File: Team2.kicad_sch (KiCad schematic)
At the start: 71 parts, among them J1 Conn_01x05, J10 Conn_01x03_MountingPin, J11 Conn_01x03_MountingPin, J12 Conn_01x03_MountingPin, J13 Conn_01x03_MountingPin, J14 Conn_01x03_MountingPin, J15 Conn_01x03_Pin, J16 Conn_01x08_Pin, J17 XT60-M, J18 XT60-M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

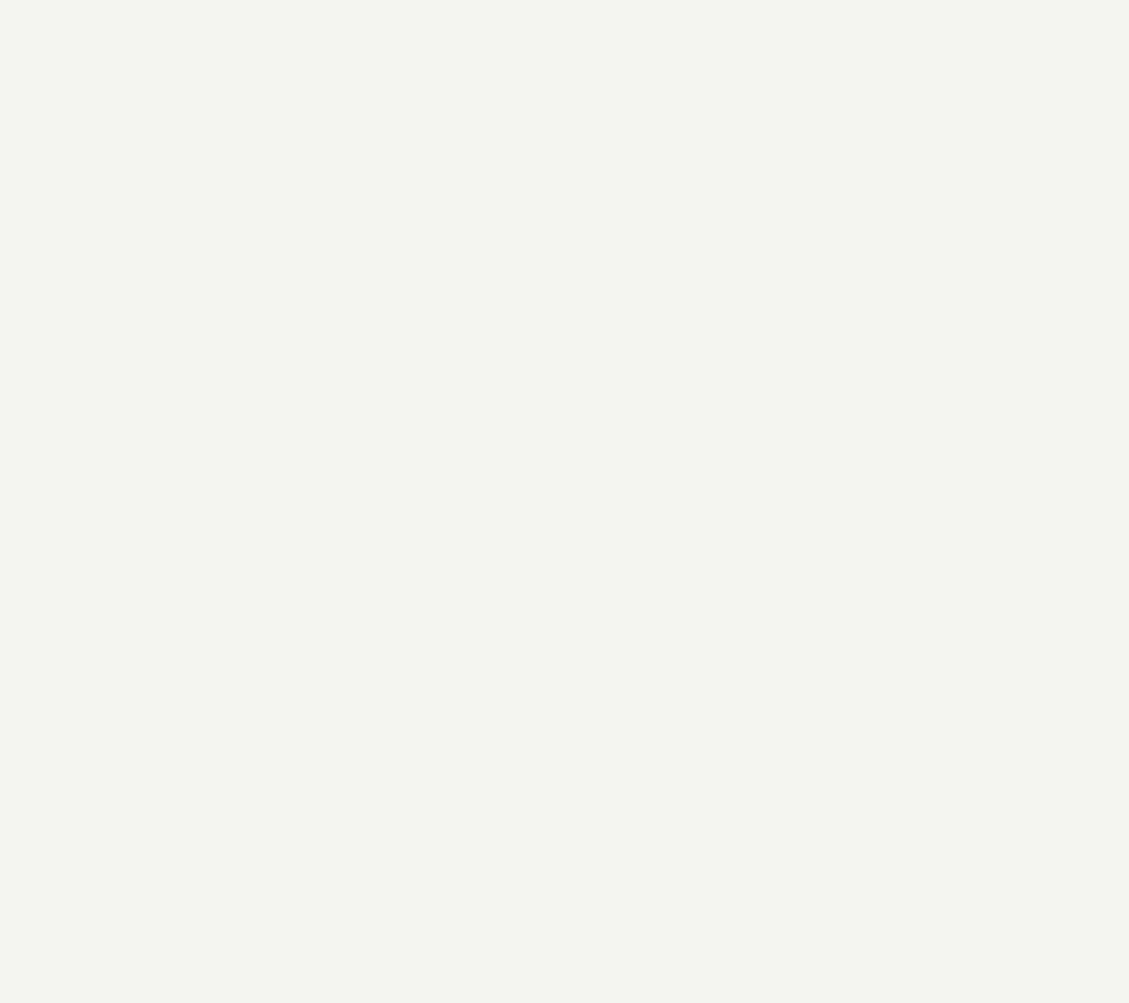
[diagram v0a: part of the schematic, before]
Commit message: schematic with vol. reg.
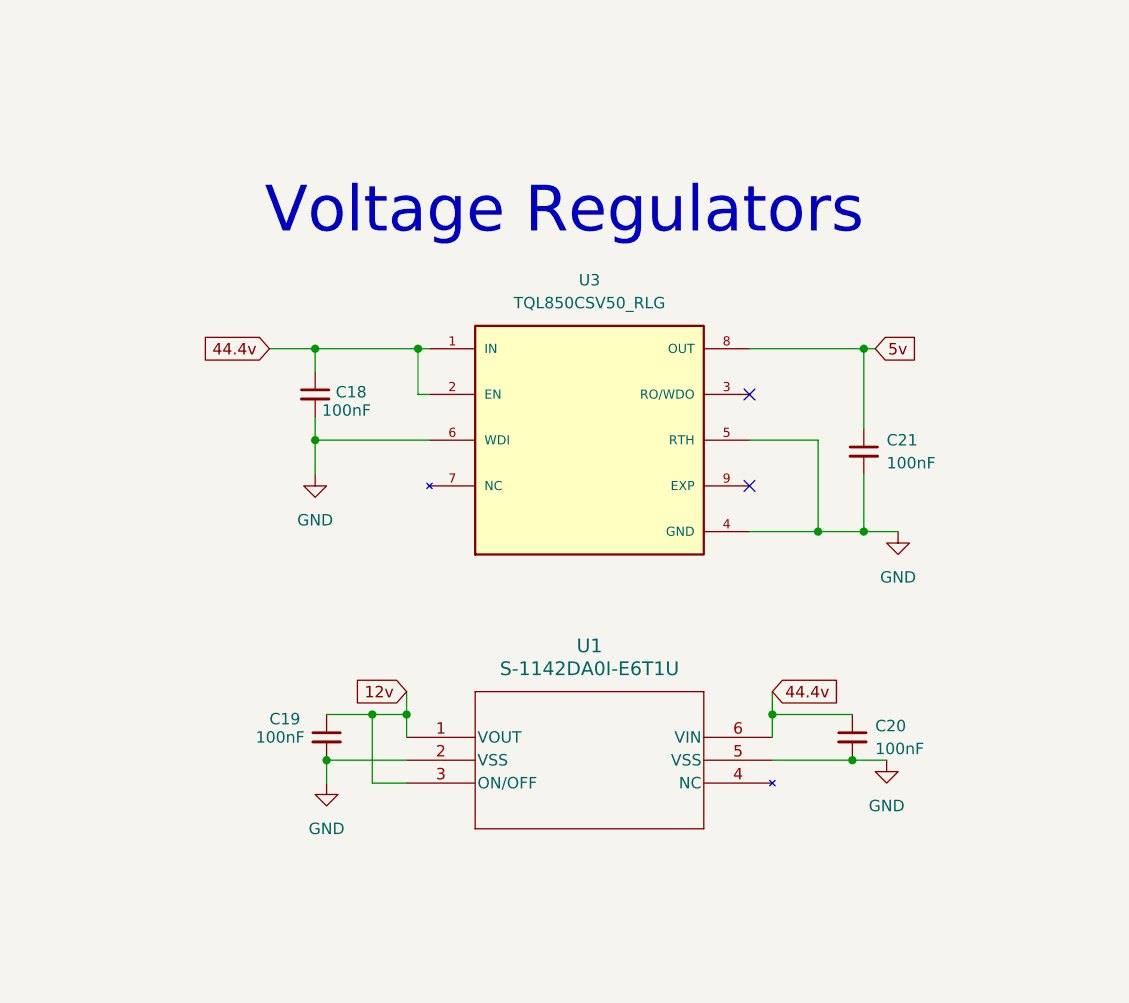
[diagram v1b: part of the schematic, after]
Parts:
- added C18, C19, C20, C21: 100nF, symbol Device:C_Small
- added U1: S-1142DA0I-E6T1U, HSOP6-A-PKG_FH006-A-P-SD-2.1_ABL, symbol voltage reg 12v:S-1142DA0I-E6T1U
- added U3: TQL850CSV50_RLG, TQL850CSV50_RLG:SOIC127P600X170-9N, symbol voltage reg. 5v:TQL850CSV50_RLG
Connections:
- net GND: now also C18.2, C19.2, C20.2, C21.2, U1.2 (VSS), U1.5 (VSS), U3.4 (GND), U3.5 (RTH), U3.6 (WDI)
- new net 12v: C19.1, U1.1 (VOUT), U1.3 (ON/OFF)
- new net 44.4v: C18.1, C20.1, U1.6 (VIN), U3.1 (IN), U3.2 (EN)
- new net 5v: C21.1, U3.8 (OUT)
- no-connect marks 3 -> 5
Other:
- note added: "Voltage Regulators"
